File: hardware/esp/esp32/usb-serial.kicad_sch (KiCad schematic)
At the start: 15 parts, among them U2 CH340C_C7464026, U9 AMS1117-3_3

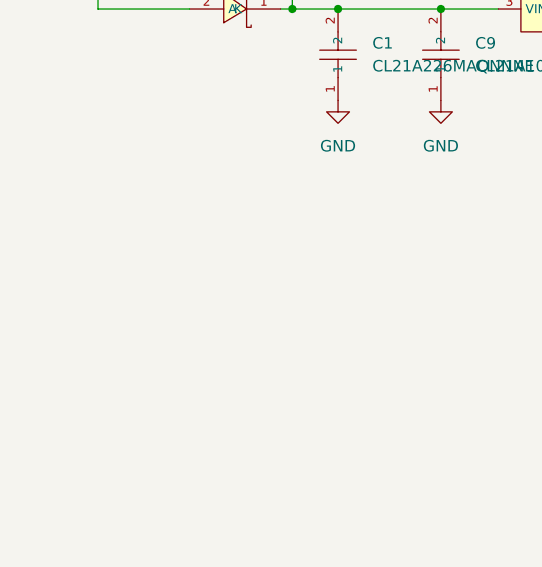
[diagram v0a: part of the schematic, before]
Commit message: Added hardware 0.2 - Added right FPC
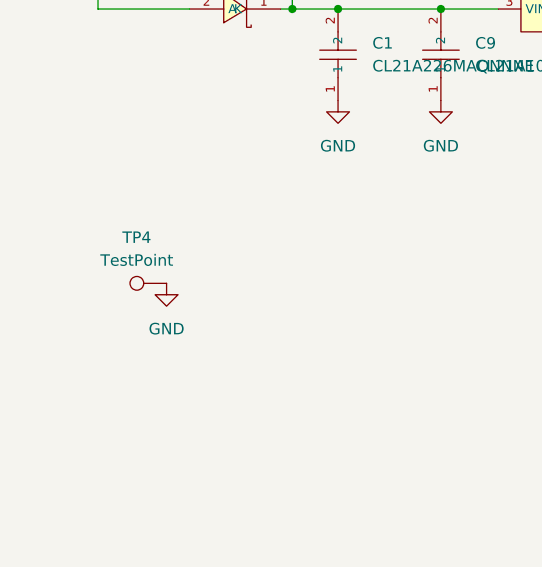
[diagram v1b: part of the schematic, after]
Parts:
- added TP4: TestPoint, TestPoint:TestPoint_Pad_2.0x2.0mm, symbol Connector:TestPoint
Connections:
- net GND: now also TP4.1
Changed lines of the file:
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@@
+	)
+	(symbol
+		(lib_id "Connector:TestPoint")
+		(at 27.94 111.76 90)
+		(unit 1)
+		(exclude_from_sim no)
+		(in_bom yes)
+		(on_board yes)
+		(dnp no)
+		(fields_autoplaced yes)
+		(property "Reference" "TP4"
+			(at 24.638 106.68 90)
+			(effects
+				(font
+					(size 1.27 1.27)
+				)
+			)
+		)
+		(property "Value" "TestPoint"
+			(at 24.638 109.22 90)
+			(effects
+				(font
+					(size 1.27 1.27)
+				)
+			)
+		)
+		(property "Footprint" "TestPoint:TestPoint_Pad_2.0x2.0mm"
+			(at 27.94 106.68 0)
+			(effects
+				(font
+					(size 1.27 1.27)
+				)
+				(hide yes)
+			)
+		)
+		(property "Datasheet" "~"
+			(at 27.94 106.68 0)
+			(effects
+				(font
+					(size 1.27 1.27)
+				)
+				(hide yes)
+			)
+		)
+		(property "Description" "test point"
+			(at 27.94 111.76 0)
+			(effects
+				(font
+					(size 1.27 1.27)
+				)
+				(hide yes)
+			)
+		)
+		(pin "1"
+		)
+		(instances
+			(project "esp32"
+				(path "/3a9f3299-35f4-4d62-9438-2986d1fa401f/586a855a-7240-4874-a1e8-0873c3df1414"
+					(reference "TP4")
+					(unit 1)
+				)
+			)
+		)
 	)
 	(symbol
@@
 					(unit 1)
 				)
+			)
+		)
+	)
+	(symbol
+		(lib_id "power:GND")
+		(at 27.94 111.76 0)
+		(unit 1)
+		(exclude_from_sim no)
+		(in_bom yes)
+		(on_board yes)
+		(dnp no)
+		(fields_autoplaced yes)
+		(property "Reference" "#PWR042"
+			(at 27.94 118.11 0)
+			(effects
+				(font
+					(size 1.27 1.27)
+				)
+				(hide yes)
+			)
+		)
+		(property "Value" "GND"
+			(at 27.94 116.84 0)
+			(effects
+				(font
+					(size 1.27 1.27)
+				)
+			)
+		)
+		(property "Footprint" ""
+			(at 27.94 111.76 0)
+			(effects
+				(font
+					(size 1.27 1.27)
+				)
+				(hide yes)
+			)
+		)
+		(property "Datasheet" ""
+			(at 27.94 111.76 0)
+			(effects
+				(font
+					(size 1.27 1.27)
+				)
+				(hide yes)
+			)
+		)
+		(property "Description" "Power symbol creates a global label with name \"GND\" , ground"
+			(at 27.94 111.76 0)
+			(effects
+				(font
+					(size 1.27 1.27)
+				)
+				(hide yes)
+			)
+		)
+		(pin "1"
+		)
+		(instances
+			(project "esp32"
+				(path "/3a9f3299-35f4-4d62-9438-2986d1fa401f/586a855a-7240-4874-a1e8-0873c3df1414"
+					(reference "#PWR042")
+					(unit 1)
+				)

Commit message: stuff
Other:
- note added: "Do these diodes mean i could safely connect USB to the board and 5v from the PSP charger at the same time? Future me question"
- note removed: "Do these diodes mean i could safely connect USB to the board and 5v from the PSP charger at the same time?"
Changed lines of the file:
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@@
 		)
 	)
-	(text "Do these diodes mean i could safely \nconnect USB to the board and 5v\nfrom the PSP charger at the same time?"
+	(text "Do these diodes mean i could safely \nconnect USB to the board and 5v\nfrom the PSP charger at the same time?\nFuture me question"
 		(exclude_from_sim no)
 		(at 39.624 58.674 0)
